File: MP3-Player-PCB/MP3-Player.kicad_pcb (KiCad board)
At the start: 4 copper layers, 50 x 50 mm, 112 parts, among them J101 Conn_ARM_SWD_TagConnect_TC2030, J201 Conn_01x02_Socket, J202 USB_C_Receptacle_USB2.0_16P, J301 Micro_SD_Card_Det1, J402 PJ-320B, Q301 AO3401A, Q302 2N7002H, Q303 AO3401A, Q304 AO3401A, Q305 2N7002H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

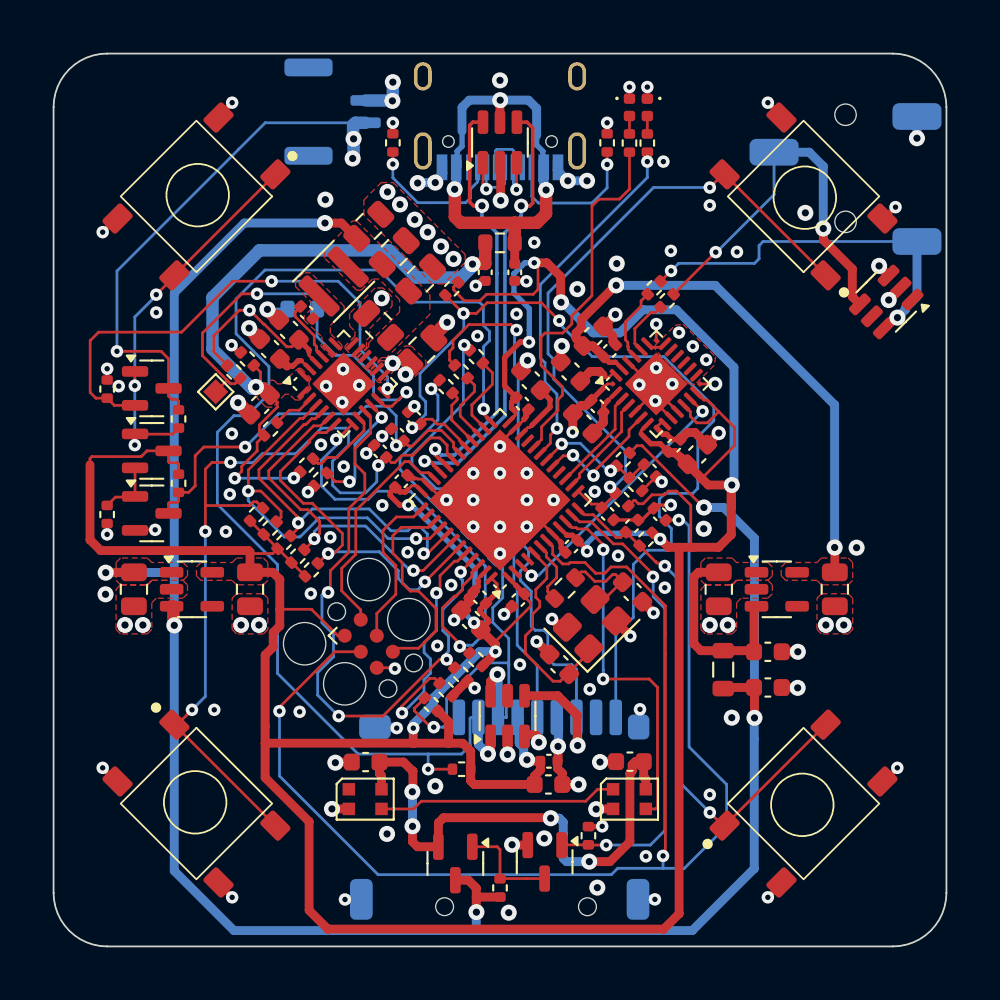
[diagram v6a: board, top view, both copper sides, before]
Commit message: Added stitching vias
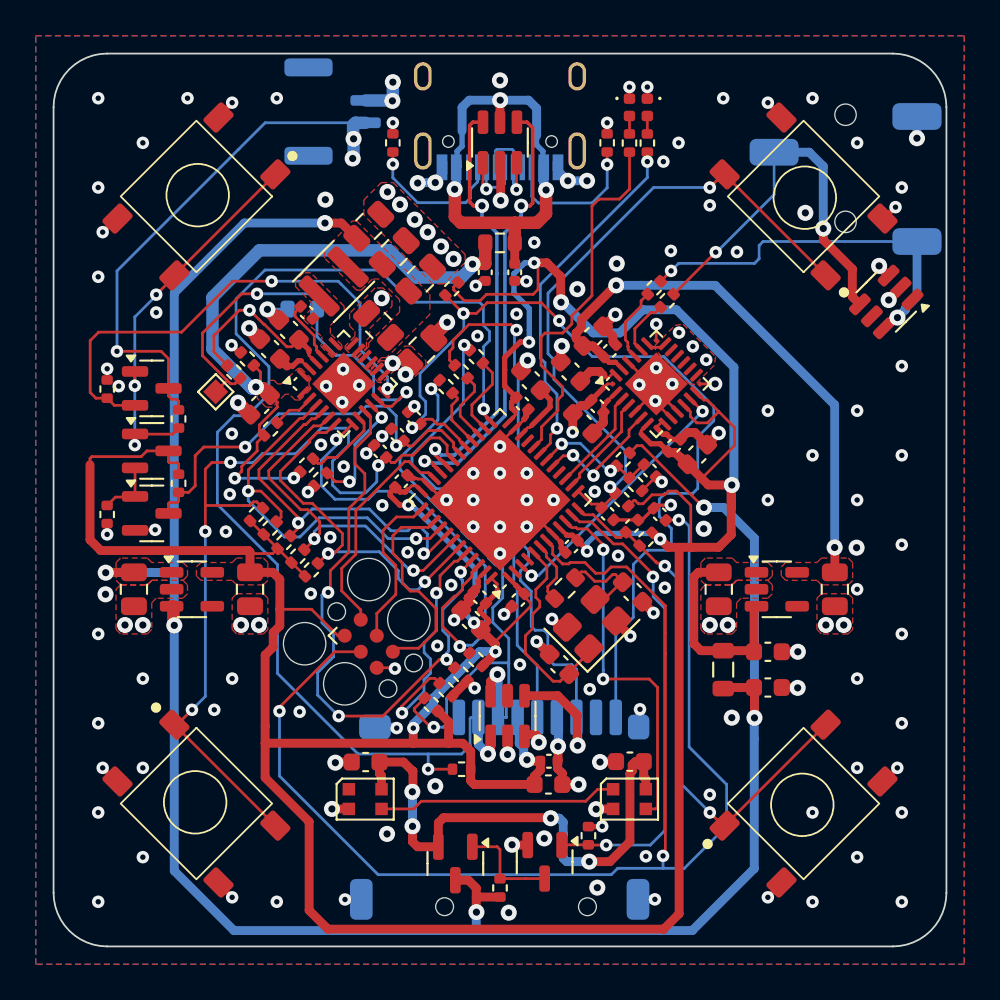
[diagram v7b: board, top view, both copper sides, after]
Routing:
- net GND: vias 149 -> 187
- added copper zone on B.Cu, net GND

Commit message: Assigning JLCPCB part #'s
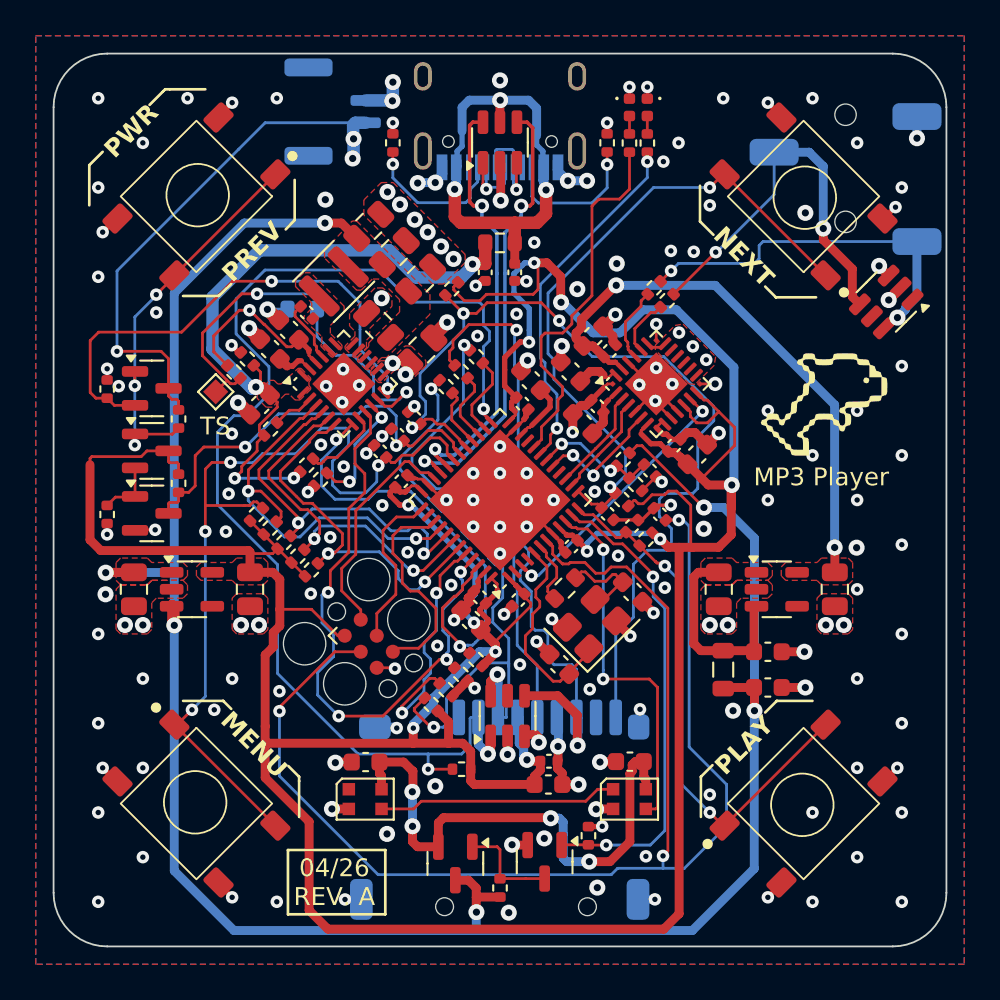
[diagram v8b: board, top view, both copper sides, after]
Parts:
- added G***: LOGO, LOGO, F.Cu at (143.0, 121.2)
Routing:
- net GND: track 106.5 -> 107.3 mm
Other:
- board text added: "04/26 REV. A"
- board text added: "MENU"
- board text added: "MP3 Player"
- board text added: "NEXT"
- board text added: "PLAY"
- board text added: "PREV"
- board text added: "PWR"
- board text added: "TS"
